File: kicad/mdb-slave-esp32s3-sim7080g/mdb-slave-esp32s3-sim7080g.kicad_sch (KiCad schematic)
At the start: 70 parts, among them J1 USB_C_Receptacle_USB2.0_16P, J2 JAE_SIM_Card_SF72S006, J3 Conn_02x11_Odd_Even, J4 Conn_Coaxial, J5 Conn_Coaxial, J6 MDB_Connector, Q1 MMBT3904, Q2 MMBT3904, Q3 MMBT3904, SW1 SW_Push, U1 ESP32-S3FH4R2, U2 SIM7080G, U3 LM2594HVM-3.3, U4 TLP785, U5 TLP785, Y1 Crystal_GND24

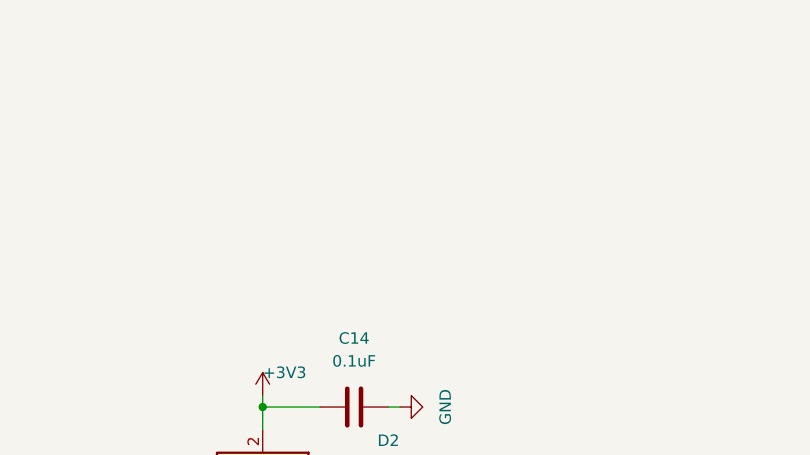
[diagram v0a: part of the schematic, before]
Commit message: slave sim7080g adding buzzer
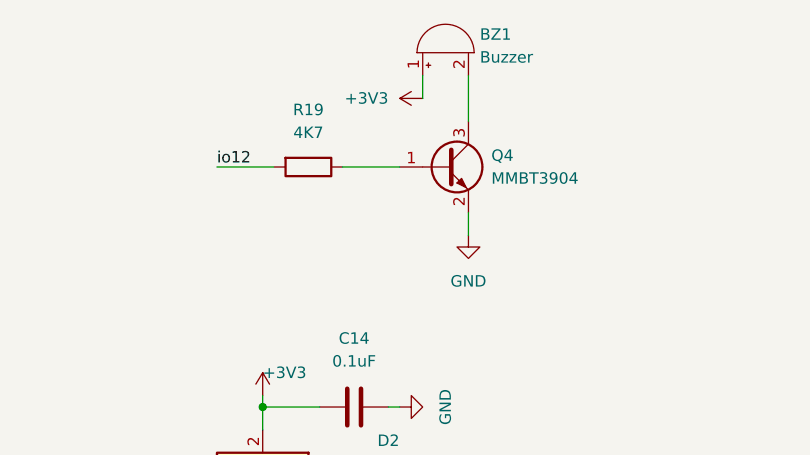
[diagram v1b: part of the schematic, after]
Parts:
- added BZ1: Buzzer, Buzzer_Beeper:Buzzer_CUI_CPT-9019S-SMT, symbol Device:Buzzer
- added Q4: MMBT3904, Package_TO_SOT_SMD:SOT-23, symbol Transistor_BJT:MMBT3904
- added R19: 4K7, Resistor_SMD:R_0603_1608Metric, symbol Device:R
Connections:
- net +3V3: now also BZ1.1 (+)
- net GND: now also Q4.2 (E)
- net io12: now also R19.2
- new net: Q4.1 (B), R19.1
- new net: BZ1.2 (-), Q4.3 (C)

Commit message: Adding buzzer and DEX level shifter
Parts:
- removed H2: MountingHole, MountingHole:MountingHole_2.1mm, symbol Mechanical:MountingHole
- removed J3: Conn_02x11_Odd_Even, Connector_PinHeader_2.54mm:PinHeader_2x11_P2.54mm_Vertical, symbol Connector_Generic:Conn_02x11_Odd_Even
- removed TP2, TP3, TP4: TestPoint, TestPoint:TestPoint_Pad_D1.0mm, symbol Connector:TestPoint
- added J7: Conn_02x08_Odd_Even, Connector_PinHeader_2.54mm:PinHeader_2x08_P2.54mm_Vertical, symbol Connector_Generic:Conn_02x08_Odd_Even
- added Q5, Q6: MMBT3904, Package_TO_SOT_SMD:SOT-23, symbol Transistor_BJT:MMBT3904
- added R20, R22: 10k, Resistor_SMD:R_0603_1608Metric, symbol Device:R
- added R21, R23: 4K7, Resistor_SMD:R_0603_1608Metric, symbol Device:R
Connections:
- net +3V3: now also C10.1, C9.1, J7.16 (Pin_16), R20.2, R21.1, R22.2, R23.1; no longer C10.2, C9.2, TP1.1
- net GND: now also C10.2, C9.2, J7.14 (Pin_14), J7.2 (Pin_2); no longer C10.1, C9.1
- net io1: now also J7.5 (Pin_5)
- net io10: now also J7.8 (Pin_8)
- net io11: now also J7.10 (Pin_10)
- net io13: now also J7.12 (Pin_12)
- net io2: now also J7.7 (Pin_7)
- net io4: now also J7.9 (Pin_9)
- net io5: now also J7.11 (Pin_11)
- net io6: now also J7.13 (Pin_13)
- net io8: now also Q5.3 (C), R20.1
- net io9: now also Q6.2 (E)
- net u0rxd: now also J7.3 (Pin_3)
- net u0txd: now also J7.1 (Pin_1)
- net vin: now also J7.15 (Pin_15)
- net at U2.42 (STATUS): now also TP1.1
- new net: Q6.1 (B), R23.2
- new net: Q5.1 (B), R21.2
- new net dex_rx: J7.4 (Pin_4), Q5.2 (E)
- new net dex_tx: J7.6 (Pin_6), Q6.3 (C), R22.1
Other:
- moved on the sheet: BZ1, C10, C14, C16, C19, C2, C20, C21, C6, C7, C8, C9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

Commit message: LCSC# C41375952 component
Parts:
- J7: LCSC# (none) -> C41375952
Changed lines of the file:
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@@
 		(at 40.64 33.02 0)
 		(unit 1)
-		(exclude_from_sim no)
+		(exclude_from_sim yes)
 		(in_bom no)
 		(on_board no)
@@
 			)
 		)
-		(property "Sim.Enable" "0"
-			(at 40.64 33.02 0)
-			(effects
-				(font
-					(size 1.27 1.27)
-				)
-				(hide yes)
-			)
-		)
 		(instances
 			(project ""
@@
 			(at 414.02 93.98 0)
 			(effects
+				(font
+					(size 1.27 1.27)
+				)
+				(hide yes)
+			)
+		)
+		(property "LCSC#" "C41375952"
+			(at 414.02 93.98 0)
+			(effects

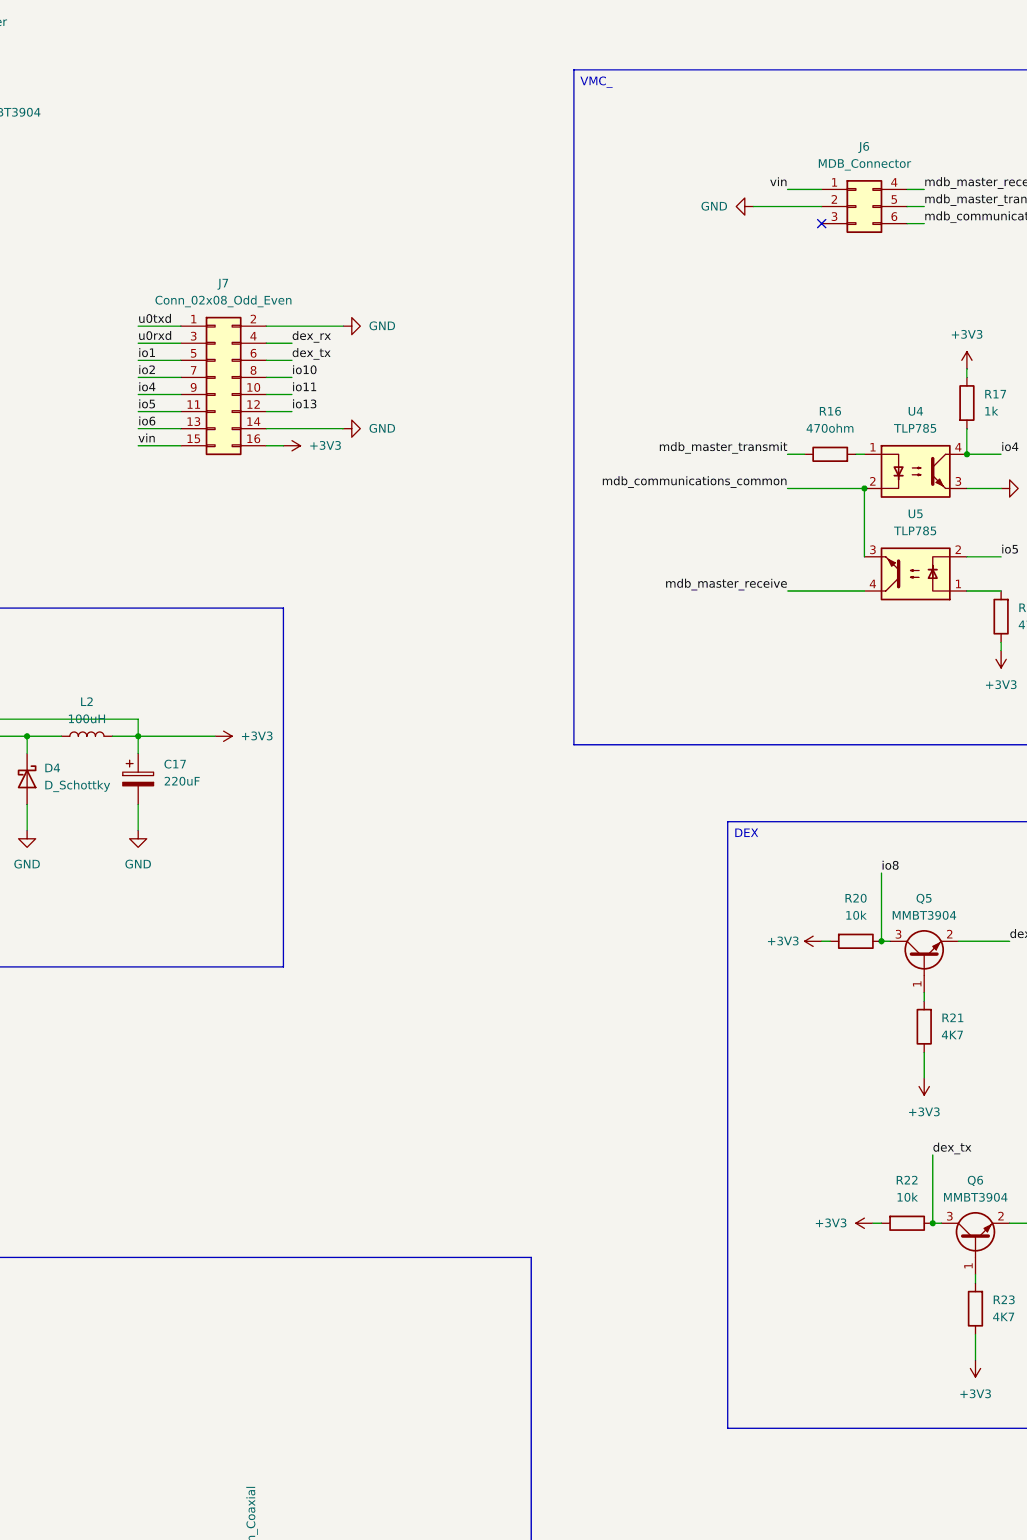
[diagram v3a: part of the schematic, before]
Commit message: Implementing JST socket to i2c and dex
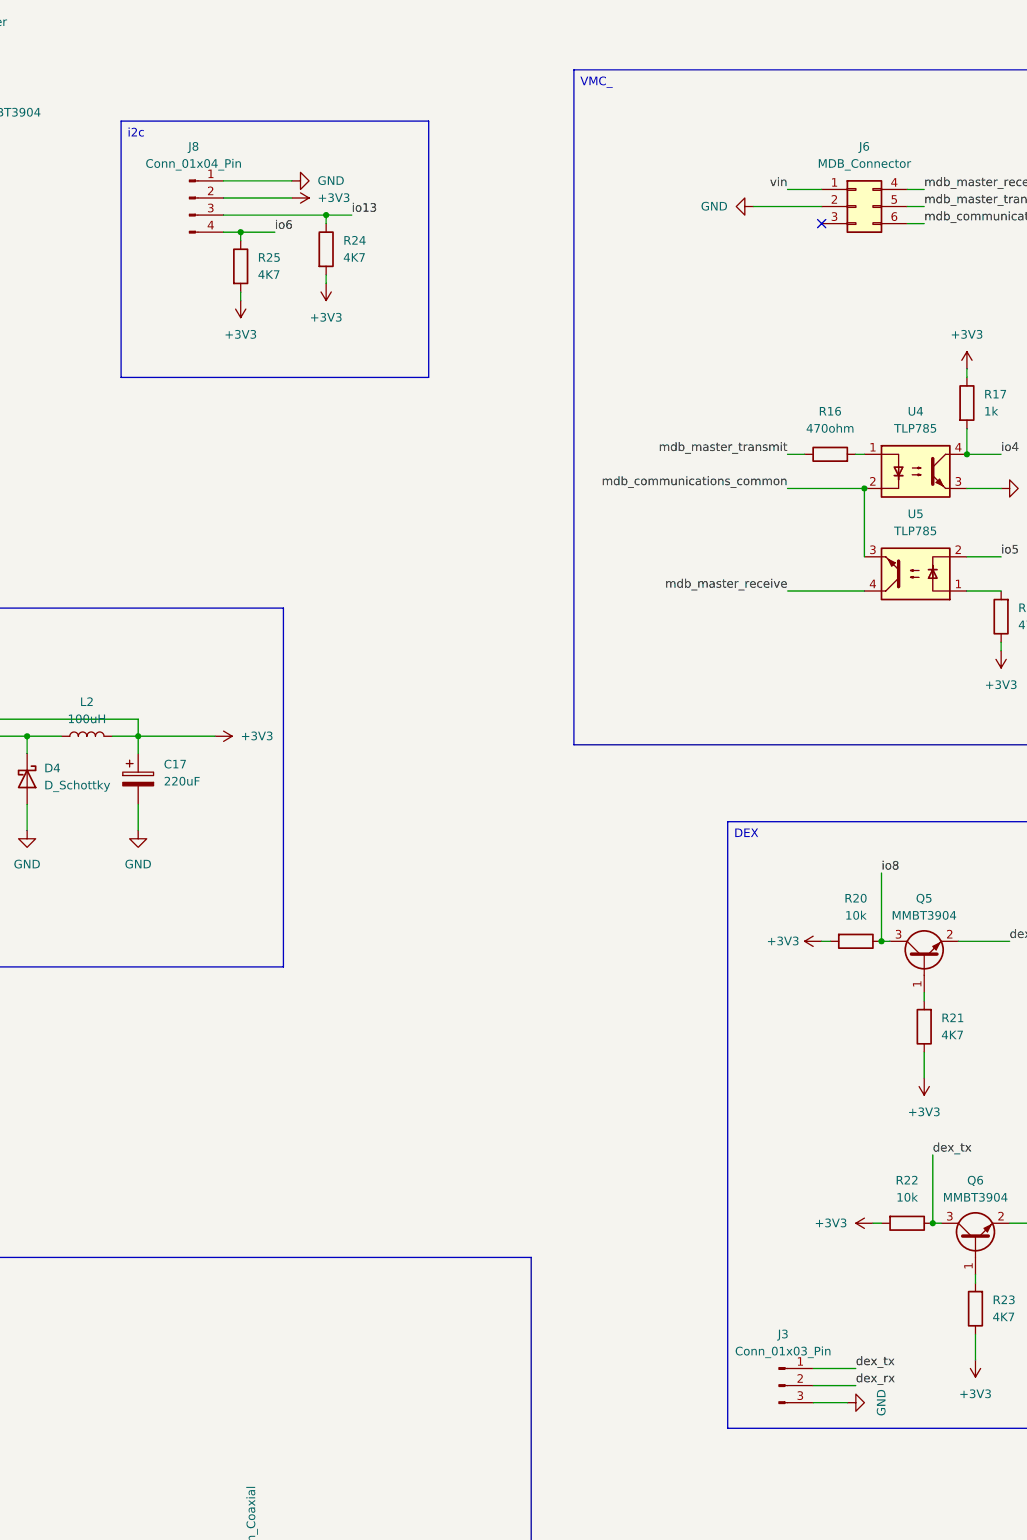
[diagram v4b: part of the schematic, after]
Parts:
- removed J7: Conn_02x08_Odd_Even, Connector_PinHeader_2.54mm:PinHeader_2x08_P2.54mm_Vertical, symbol Connector_Generic:Conn_02x08_Odd_Even
- added J3: Conn_01x03_Pin, Connector_JST:JST_XH_B3B-XH-A_1x03_P2.50mm_Vertical, symbol Connector:Conn_01x03_Pin
- added J8: Conn_01x04_Pin, Connector_JST:JST_EH_B4B-EH-A_1x04_P2.50mm_Vertical, symbol Connector:Conn_01x04_Pin
- added R24, R25: 4K7, Resistor_SMD:R_0603_1608Metric, symbol Device:R
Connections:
- net +3V3: now also J8.2 (Pin_2), R24.2, R25.2
- net GND: now also J3.3 (Pin_3), J8.1 (Pin_1)
- net dex_rx: now also J3.2 (Pin_2)
- net dex_tx: now also J3.1 (Pin_1)
- net io13: now also J8.3 (Pin_3), R24.1
- net io6: now also J8.4 (Pin_4), R25.1

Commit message: Refacting i2c pinout
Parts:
- added J9: Conn_01x02_Pin, Connector_JST:JST_EH_B2B-EH-A_1x02_P2.50mm_Vertical, symbol Connector:Conn_01x02_Pin
- added Q7: MMBT3904, Package_TO_SOT_SMD:SOT-23, symbol Transistor_BJT:MMBT3904
- added R27: 4K7, Resistor_SMD:R_0603_1608Metric, symbol Device:R
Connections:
- net GND: now also J9.2 (Pin_2), Q7.2 (E)
- net io10: now also J8.3 (Pin_3), R24.1
- net io11: now also J8.4 (Pin_4), R25.1
- net io13: now also R27.1; no longer J8.3 (Pin_3), R24.1
- net io6: no longer J8.4 (Pin_4), R25.1
- new net: Q7.1 (B), R27.2
- new net: J9.1 (Pin_1), Q7.3 (C)
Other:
- moved on the sheet: BZ1, C10, C15, C17, C6, C7, C8, C9, D1, D4, FB1, J1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

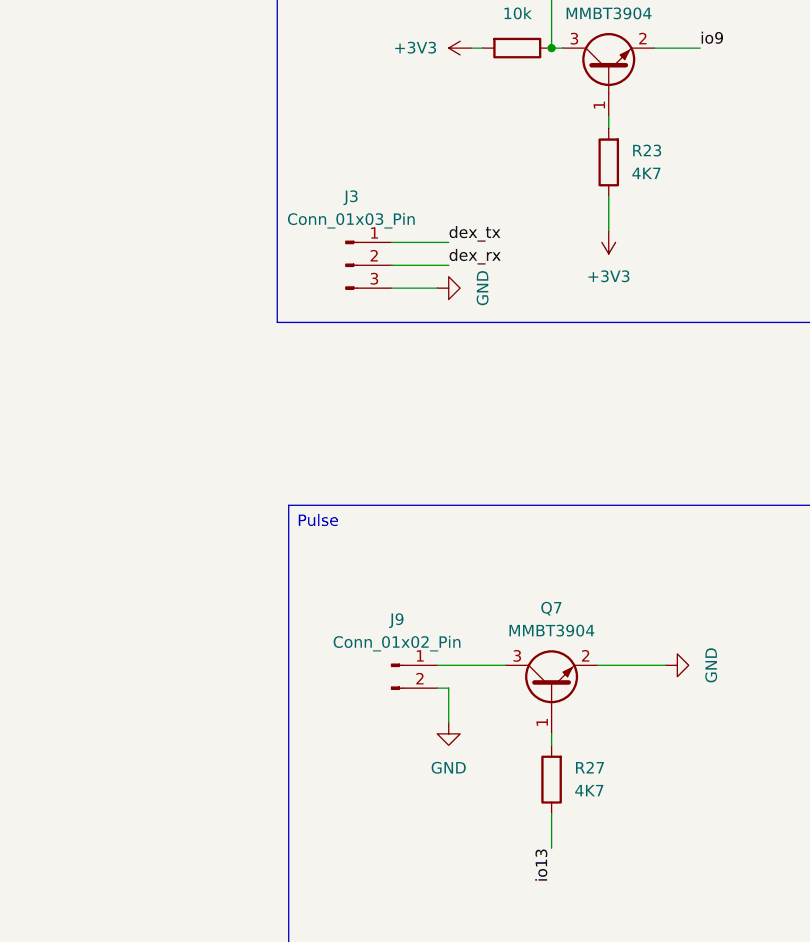
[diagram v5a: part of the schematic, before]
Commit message: kicad jst sockets to dex/pulse/i2c
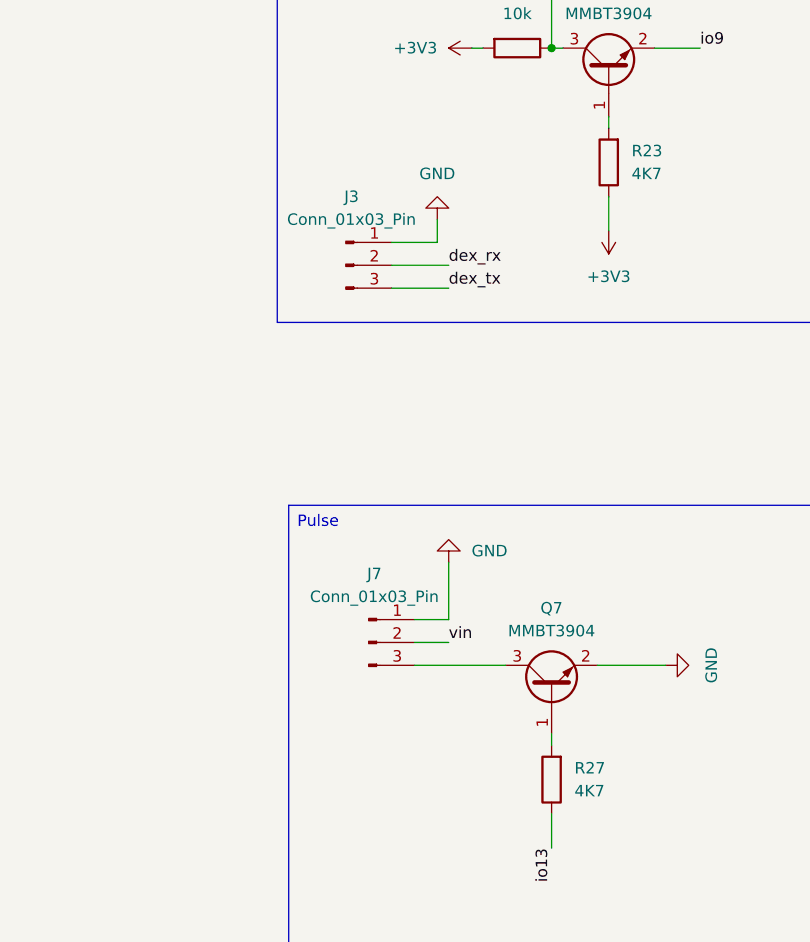
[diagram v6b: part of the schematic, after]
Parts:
- removed J9: Conn_01x02_Pin, Connector_JST:JST_EH_B2B-EH-A_1x02_P2.50mm_Vertical, symbol Connector:Conn_01x02_Pin
- added J7: Conn_01x03_Pin, Connector_JST:JST_PH_B3B-PH-K_1x03_P2.00mm_Vertical, symbol Connector:Conn_01x03_Pin
- J3: footprint Connector_JST:JST_XH_B3B-XH-A_1x03_P2.50mm_Vertical -> Connector_JST:JST_PH_B3B-PH-K_1x03_P2.00mm_Vertical; LCSC# C144394 -> C131339
- J8: footprint Connector_JST:JST_EH_B4B-EH-A_1x04_P2.50mm_Vertical -> Connector_JST:JST_PH_B4B-PH-K_1x04_P2.00mm_Vertical; LCSC# C144395 -> C131334
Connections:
- net GND: now also J3.1 (Pin_1), J7.1 (Pin_1); no longer J3.3 (Pin_3)
- net dex_tx: now also J3.3 (Pin_3); no longer J3.1 (Pin_1)
- net vin: now also J7.2 (Pin_2)
- net at Q7.3 (C): now also J7.3 (Pin_3)

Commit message: routing...
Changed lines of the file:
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@@
 		)
 	)
-	(text_box "io1\nio2\nio4 	-> 	mdb/rx\nio5 	-> 	mdb/tx\nio6 	\nio7		->	thermistor\nio8 	-> 	dex/rx\nio9 	-> 	dex/tx\nio10 	->	i2c/scl\nio11	->	i2c/sda\nio12 	-> 	buzzer\nio13 	-> 	pulse\nio14 	-> 	sim7080g/pwrk\nio17 	-> 	sim7080g/tx\nio18 	-> 	sim7080g/rx\nio21 	->	led	\n"
+	(text_box "MCU <-> sim7080G"
 		(exclude_from_sim no)
-		(at 31.75 168.91 0)
-		(size 38.1 34.29)
+		(at 52.07 294.64 0)
+		(size 63.5 82.55)
 		(margins 0.9525 0.9525 0.9525 0.9525)
 		(stroke
@@
 		)
 	)
-	(text_box "MCU <-> sim7080G"
+	(text_box "io1\nio2\nio4 	-> 	mdb/rx\nio5 	-> 	mdb/tx\nio6 	\nio7		->	thermistor\nio8 	-> 	dex/rx\nio9 	-> 	dex/tx\nio10 	->	i2c/sda\nio11	->	i2c/scl\nio12 	-> 	buzzer\nio13 	-> 	pulse\nio14 	-> 	sim7080g/pwrk\nio17 	-> 	sim7080g/tx\nio18 	-> 	sim7080g/rx\nio21 	->	led	\n"
 		(exclude_from_sim no)
-		(at 52.07 294.64 0)
-		(size 63.5 82.55)
+		(at 30.48 168.91 0)
+		(size 38.1 34.29)
 		(margins 0.9525 0.9525 0.9525 0.9525)
 		(stroke
